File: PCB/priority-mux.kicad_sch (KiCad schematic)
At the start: 7 parts, among them U2 LTC4417IGN#TRPBF

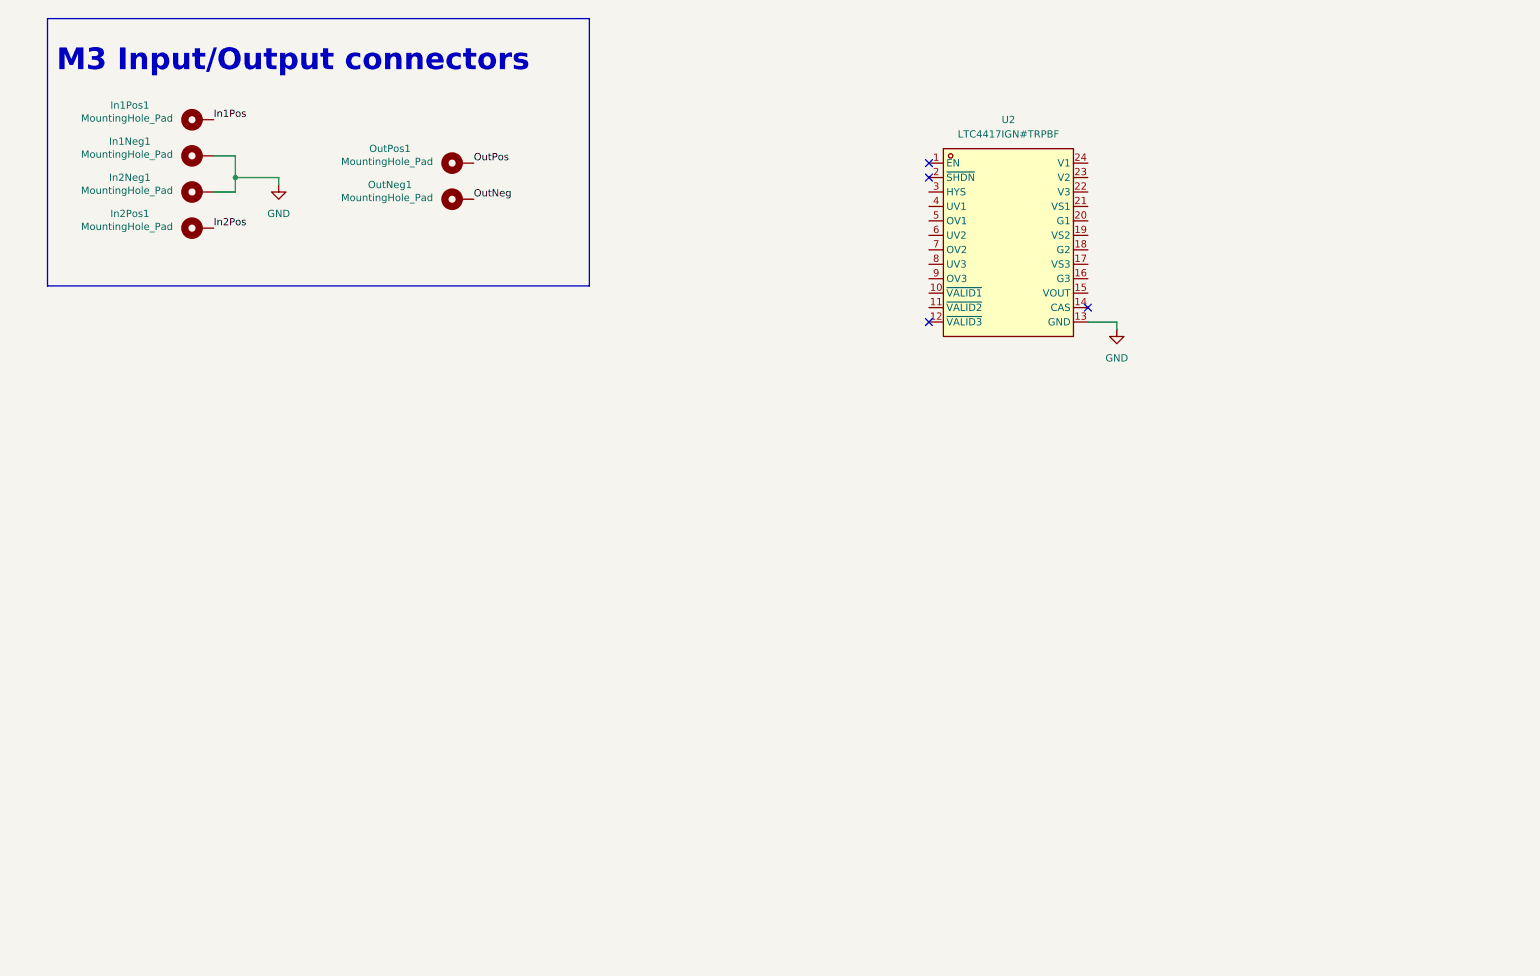
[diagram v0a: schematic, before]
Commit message: Added circuitry for power mux
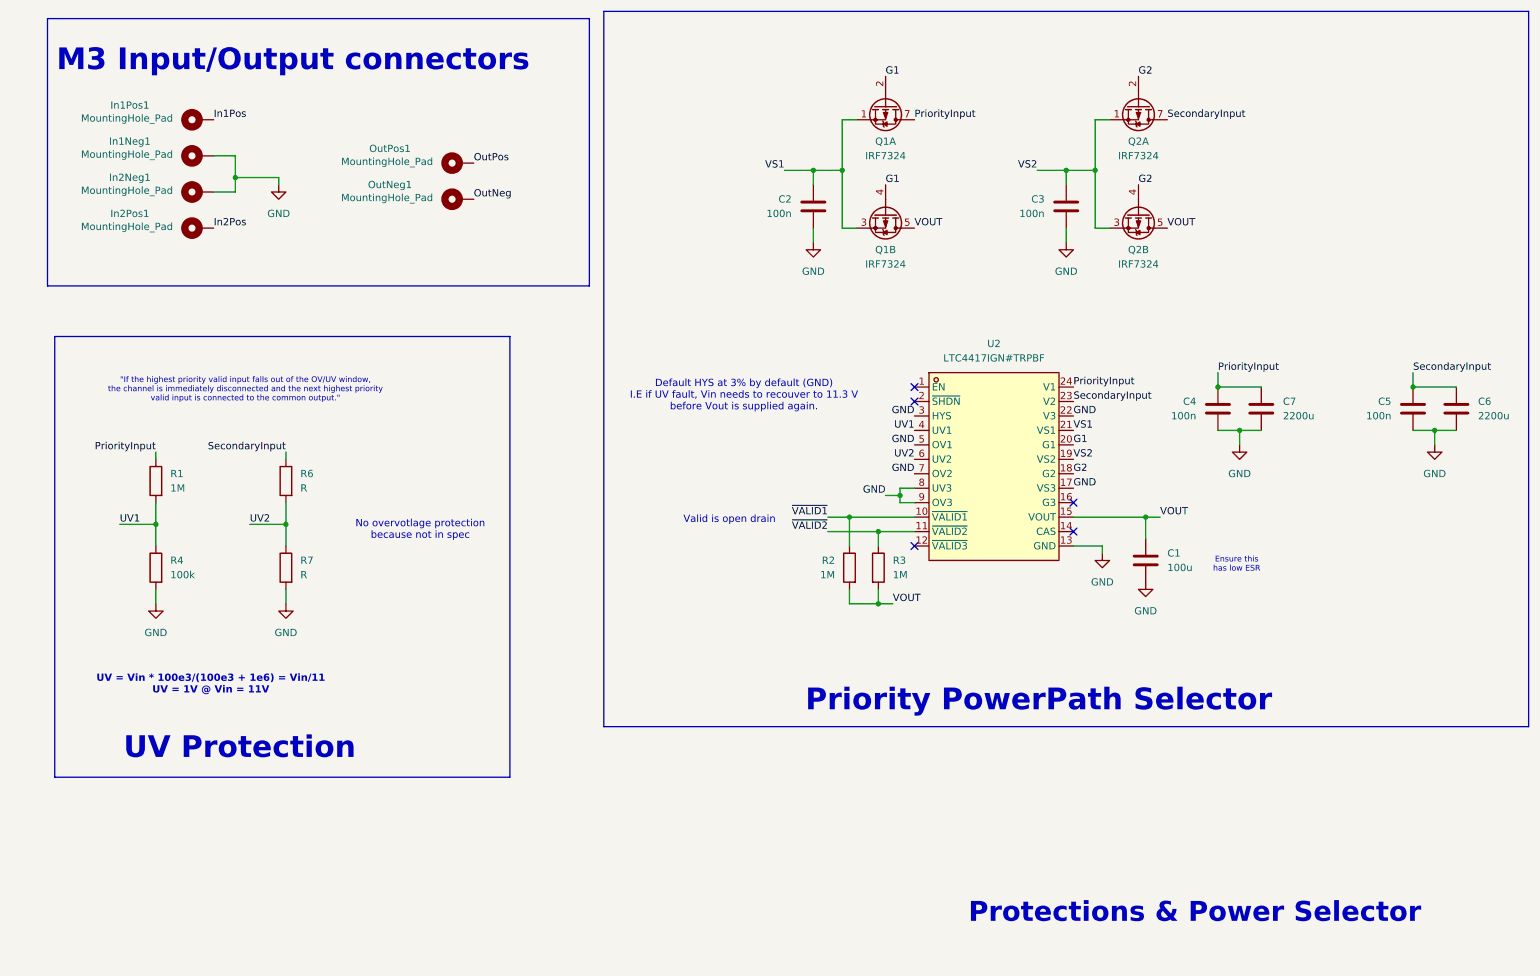
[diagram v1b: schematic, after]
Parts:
- added C1: 100u, symbol Device:C
- added C2, C3, C4, C5: 100n, symbol Device:C
- added C6, C7: 2200u, symbol Device:C
- added Q1, Q2: IRF7324, Package_SO:SOIC-8_3.9x4.9mm_P1.27mm, symbol Transistor_FET:IRF7324
- added R1, R2, R3: 1M, symbol Device:R
- added R4: 100k, symbol Device:R
- added R6, R7: R, symbol Device:R
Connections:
- net GND: now also U2.17 (VS3), U2.22 (V3), U2.3 (HYS), U2.5 (OV1), U2.7 (OV2), U2.8 (UV3), U2.9 (OV3), C1.2, C2.2, C3.2, C4.2, C5.2, C6.2, C7.2, R4.2, R7.2
- net ~{VALID1}: now reaches U2.10 (~{VALID1})
- net ~{VALID1}: now also R2.1
- net ~{VALID2}: now reaches U2.11 (~{VALID2})
- net ~{VALID2}: now also R3.1
- net VOUT: now reaches U2.15 (VOUT)
- net VOUT: now also C1.1, Q1.5 (D2), Q1.6 (D2), Q2.5 (D2), Q2.6 (D2), R2.2, R3.2
- net G2: now reaches U2.18 (G2)
- net G2: now also Q2.2 (G1), Q2.4 (G2)
- net VS2: now reaches U2.19 (VS2)
- net VS2: now also C3.1, Q2.1 (S1), Q2.3 (S2)
- net G1: now reaches U2.20 (G1)
- net G1: now also Q1.2 (G1), Q1.4 (G2)
- net VS1: now reaches U2.21 (VS1)
- net VS1: now also C2.1, Q1.1 (S1), Q1.3 (S2)
- net SecondaryInput: now reaches U2.23 (V2)
- net SecondaryInput: now also C5.1, C6.1, Q2.7 (D1), Q2.8 (D1), R6.1
- net PriorityInput: now reaches U2.24 (V1)
- net PriorityInput: now also C4.1, C7.1, Q1.7 (D1), Q1.8 (D1), R1.1
- net UV1: now reaches U2.4 (UV1)
- net UV1: now also R1.2, R4.1
- net UV2: now reaches U2.6 (UV2)
- net UV2: now also R6.2, R7.1
- no-connect marks 4 -> 5
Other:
- note added: ""If the highest priority valid input falls out of the OV/UV window, the channel is immediately disconnected and the next highest priority valid input is connected to the common output.""
- note added: "Default HYS at 3% by default (GND) I.E if UV fault, Vin needs to recouver to 11.3 V before Vout is supplied again."
- note added: "Ensure this has low ESR"
- note added: "No overvotlage protection because not in spec"
- note added: "Priority PowerPath Selector"
- note added: "Protections & Power Selector"
- note added: "UV = Vin * 100e3/(100e3 + 1e6) = Vin/11 UV = 1V @ Vin = 11V"
- note added: "UV Protection"
- note added: "Valid is open drain"
- moved on the sheet: U2

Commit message: Minor changes to schematic
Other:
- note added: "Power Selector"
- note removed: "Protections & Power Selector"
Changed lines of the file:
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@@
 		)
 	)
-	(text "Protections & Power Selector"
+	(text "Power Selector"
 		(exclude_from_sim no)
 		(at 219.456 175.006 0)

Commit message: Updated schematic and created 3D assembly to check mechanical clearances and review with Thomas.
To-do, clarify where the input and output ports should be.
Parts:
- removed In2Neg1: MountingHole_Pad, symbol Mechanical:MountingHole_Pad
- added A1, A2: MountingHole_Pad, footprints:MG_ThermalTab_M3, symbol Mechanical:MountingHole_Pad
- added F1, F2: Fuse, Fuse:Fuse_0805_2012Metric_Pad1.15x1.40mm_HandSolder, symbol Device:Fuse
- C1, C2, C3, C4, C5: footprint (none) -> Capacitor_SMD:C_0603_1608Metric
- C6, C7: footprint (none) -> Capacitor_THT:C_Radial_D10.0mm_H12.5mm_P5.00mm
- INPUT_GND1: renamed from In1Neg1; footprint (none) -> footprints:MG_ThermalTab_M3
- In1Pos1, In2Pos1, OutNeg1, OutPos1: footprint (none) -> footprints:MG_ThermalTab_M3
- R1: footprint (none) -> Resistor_SMD:R_0805_2012Metric
- R2: footprint (none) -> Resistor_SMD:R_0201_0603Metric
- R3, R4: footprint (none) -> Resistor_SMD:R_0603_1608Metric
- R6: value R -> 1M; footprint (none) -> Resistor_SMD:R_0603_1608Metric
- R7: value R -> 100k; footprint (none) -> Resistor_SMD:R_0603_1608Metric
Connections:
- net GND: now also A2.1
- net In1Pos: now also F2.1
- net In2Pos: now also F1.1
- net PriorityInput: now also F1.2
- net SecondaryInput: now also F2.2
- net VOUT renamed Vmux
- new net AccessoryBus: A1.1
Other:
- note added: "Accessory Outputs"
- moved on the sheet: C4, C5, C6, C7, R1, R4, R6, R7
